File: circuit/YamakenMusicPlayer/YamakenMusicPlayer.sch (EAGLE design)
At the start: 24 parts, among them J1 DCJ0202, J2 AJ-1780, U1 NJM2396F33, U2 AE-ESP-WROOM-02

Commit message: 表記の修正
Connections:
- net DAC_GND: now also U$1.DAC_GND; no longer U$1.GND_1
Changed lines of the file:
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@@
 <part name="C4" library="rcl" library_urn="urn:adsk.eagle:library:334" deviceset="C-EU" device="050-024X044" package3d_urn="urn:adsk.eagle:package:23643/1" value="10μF"/>
 <part name="C5" library="rcl" library_urn="urn:adsk.eagle:library:334" deviceset="C-EU" device="050-024X044" package3d_urn="urn:adsk.eagle:package:23643/1" value="0.1μF"/>
-<part name="SUPPLY12" library="supply2" library_urn="urn:adsk.eagle:library:372" deviceset="GND" device=""/>
 <part name="J2" library="SamacSys_Parts" deviceset="AJ-1780" device=""/>
 <part name="SUPPLY14" library="supply2" library_urn="urn:adsk.eagle:library:372" deviceset="V+" device=""/>
@@
 <part name="JP2" library="pinhead" library_urn="urn:adsk.eagle:library:325" deviceset="PINHD-1X3" device="" package3d_urn="urn:adsk.eagle:package:22458/2" value="VOLUME_VR"/>
 <part name="U$1" library="DFPlayer_v1" deviceset="DFPLAYERMINI" device=""/>
+<part name="SUPPLY12" library="supply2" library_urn="urn:adsk.eagle:library:372" deviceset="GND" device=""/>
 </parts>
 <sheets>
@@
 <attribute name="VALUE" x="171.577" y="150.368" size="1.778" layer="96"/>
 </instance>
-<instance part="SUPPLY12" gate="GND" x="124.46" y="7.62" smashed="yes" rot="MR0">
-<attribute name="VALUE" x="47.625" y="47.625" size="1.778" layer="96" rot="MR0"/>
-</instance>
 <instance part="J2" gate="G$1" x="43.18" y="30.48" smashed="yes" rot="MR0">
 <attribute name="NAME" x="26.67" y="38.1" size="1.778" layer="95" rot="MR0" align="center-left"/>
@@
 <attribute name="NAME" x="86.36" y="38.862" size="1.4224" layer="95"/>
 <attribute name="VALUE" x="86.36" y="12.7" size="1.4224" layer="96"/>
+</instance>
+<instance part="SUPPLY12" gate="GND" x="124.46" y="7.62" smashed="yes">
+<attribute name="VALUE" x="122.555" y="4.445" size="1.778" layer="96"/>
 </instance>
 </instances>
@@
 </segment>
 <segment>
-<wire x1="116.84" y1="20.32" x2="124.46" y2="20.32" width="0.1524" layer="91"/>
-<wire x1="124.46" y1="20.32" x2="124.46" y2="10.16" width="0.1524" layer="91"/>
-<pinref part="SUPPLY12" gate="GND" pin="GND"/>
-<pinref part="U$1" gate="G$1" pin="GND_2"/>
-</segment>
-<segment>
 <pinref part="C6" gate="G$1" pin="1"/>
 <wire x1="53.34" y1="50.8" x2="48.26" y2="50.8" width="0.1524" layer="91"/>
@@
 <wire x1="175.26" y1="55.88" x2="182.88" y2="55.88" width="0.1524" layer="91"/>
 </segment>
+<segment>
+<wire x1="116.84" y1="20.32" x2="124.46" y2="20.32" width="0.1524" layer="91"/>
+<wire x1="124.46" y1="20.32" x2="124.46" y2="10.16" width="0.1524" layer="91"/>
+<pinref part="U$1" gate="G$1" pin="GND_2"/>
+<pinref part="SUPPLY12" gate="GND" pin="GND"/>
+</segment>
 </net>
 <net name="N$1" class="0">
@@
 <wire x1="48.26" y1="30.48" x2="48.26" y2="20.32" width="0.1524" layer="91"/>
 <wire x1="81.28" y1="20.32" x2="48.26" y2="20.32" width="0.1524" layer="91"/>
-<pinref part="U$1" gate="G$1" pin="GND_1"/>
-</segment>
-</net>
+<pinref part="U$1" gate="G$1" pin="DAC_GND"/>
+</segment>
+</net>

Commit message: 表記の修正
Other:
- note added: "A) 電源回路部"
- note added: "B) 制御IC部"
- note added: "C) プレイヤーIC部"
- note removed: "A 電源回路部"
- note removed: "B 制御IC部"
- note removed: "C プレイヤーIC部"
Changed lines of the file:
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@@
 <text x="241.3" y="24.13" size="1.778" layer="94">Designed by
 16TE014 中禮 大貴</text>
-<text x="106.68" y="170.18" size="2.54" layer="94">B 制御IC部</text>
-<text x="12.7" y="170.18" size="2.54" layer="94">A 電源回路部</text>
-<text x="15.24" y="66.04" size="2.54" layer="94">C プレイヤーIC部</text>
+<text x="106.68" y="170.18" size="2.54" layer="94">B) 制御IC部</text>
+<text x="12.7" y="170.18" size="2.54" layer="94">A) 電源回路部</text>
+<text x="15.24" y="66.04" size="2.54" layer="94">C) プレイヤーIC部</text>
 </plain>
 <instances>

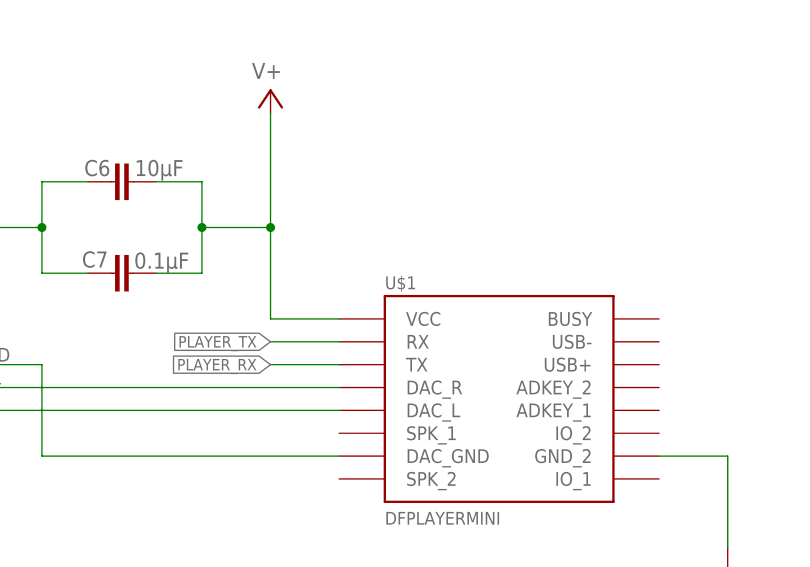
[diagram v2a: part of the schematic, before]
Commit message: U3の表記を追加
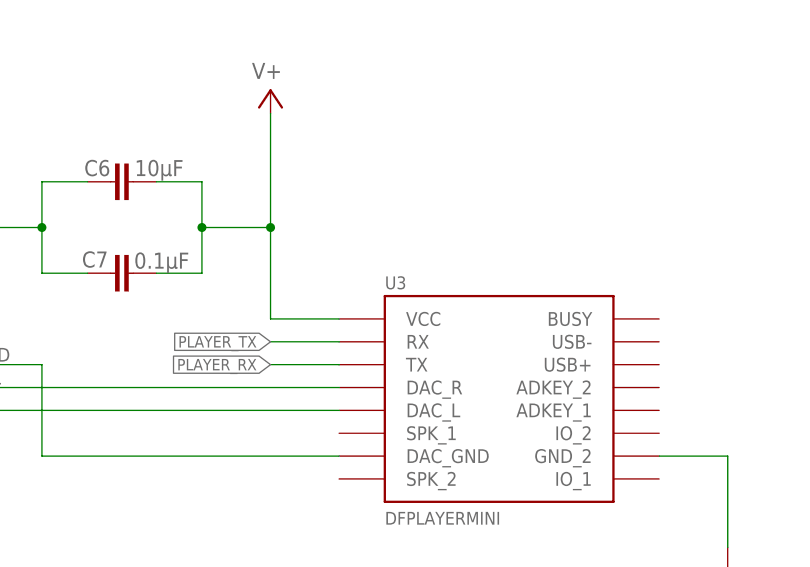
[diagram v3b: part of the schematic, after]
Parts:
- renumbered U$1 to U3
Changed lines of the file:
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@@
 <part name="SUPPLY20" library="supply2" library_urn="urn:adsk.eagle:library:372" deviceset="GND" device=""/>
 <part name="JP2" library="pinhead" library_urn="urn:adsk.eagle:library:325" deviceset="PINHD-1X3" device="" package3d_urn="urn:adsk.eagle:package:22458/2" value="VOLUME_VR"/>
-<part name="U$1" library="DFPlayer_v1" deviceset="DFPLAYERMINI" device=""/>
+<part name="U3" library="DFPlayer_v1" deviceset="DFPLAYERMINI" device=""/>
 <part name="SUPPLY12" library="supply2" library_urn="urn:adsk.eagle:library:372" deviceset="GND" device=""/>
 </parts>
@@
 <attribute name="VALUE" x="179.07" y="50.8" size="1.778" layer="96"/>
 </instance>
-<instance part="U$1" gate="G$1" x="99.06" y="25.4" smashed="yes">
+<instance part="U3" gate="G$1" x="99.06" y="25.4" smashed="yes">
 <attribute name="NAME" x="86.36" y="38.862" size="1.4224" layer="95"/>
 <attribute name="VALUE" x="86.36" y="12.7" size="1.4224" layer="96"/>
@@
 <junction x="66.04" y="45.72"/>
 <junction x="73.66" y="45.72"/>
-<pinref part="U$1" gate="G$1" pin="VCC"/>
+<pinref part="U3" gate="G$1" pin="VCC"/>
 </segment>
 <segment>
@@
 <wire x1="116.84" y1="20.32" x2="124.46" y2="20.32" width="0.1524" layer="91"/>
 <wire x1="124.46" y1="20.32" x2="124.46" y2="10.16" width="0.1524" layer="91"/>
-<pinref part="U$1" gate="G$1" pin="GND_2"/>
+<pinref part="U3" gate="G$1" pin="GND_2"/>
 <pinref part="SUPPLY12" gate="GND" pin="GND"/>
 </segment>
@@
 <wire x1="81.28" y1="33.02" x2="73.66" y2="33.02" width="0.1524" layer="91"/>
 <label x="73.66" y="33.02" size="1.27" layer="95" rot="MR0" xref="yes"/>
-<pinref part="U$1" gate="G$1" pin="RX"/>
+<pinref part="U3" gate="G$1" pin="RX"/>
 </segment>
 </net>
@@
 <wire x1="81.28" y1="30.48" x2="73.66" y2="30.48" width="0.1524" layer="91"/>
 <label x="73.66" y="30.48" size="1.27" layer="95" rot="MR0" xref="yes"/>
-<pinref part="U$1" gate="G$1" pin="TX"/>
+<pinref part="U3" gate="G$1" pin="TX"/>
 </segment>
 </net>
@@
 <pinref part="J2" gate="G$1" pin="R_1"/>
 <wire x1="81.28" y1="27.94" x2="43.18" y2="27.94" width="0.1524" layer="91"/>
-<pinref part="U$1" gate="G$1" pin="DAC_R"/>
+<pinref part="U3" gate="G$1" pin="DAC_R"/>
 </segment>
 </net>
@@
 <pinref part="J2" gate="G$1" pin="L_1"/>
 <wire x1="81.28" y1="25.4" x2="43.18" y2="25.4" width="0.1524" layer="91"/>
-<pinref part="U$1" gate="G$1" pin="DAC_L"/>
+<pinref part="U3" gate="G$1" pin="DAC_L"/>
 </segment>
 </net>
@@
 <wire x1="48.26" y1="30.48" x2="48.26" y2="20.32" width="0.1524" layer="91"/>
 <wire x1="81.28" y1="20.32" x2="48.26" y2="20.32" width="0.1524" layer="91"/>
-<pinref part="U$1" gate="G$1" pin="DAC_GND"/>
-</segment>
-</net>
+<pinref part="U3" gate="G$1" pin="DAC_GND"/>
+</segment>
+</net>

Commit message: ファイルの差し替え
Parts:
- J1: value DCJ0202 -> MJ-179PH
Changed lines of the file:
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@@
 <part name="C2" library="rcl" library_urn="urn:adsk.eagle:library:334" deviceset="CPOL-EU" device="E2.5-7" package3d_urn="urn:adsk.eagle:package:23345/1" value="22μF"/>
 <part name="3V3" library="supply2" library_urn="urn:adsk.eagle:library:372" deviceset="V+" device=""/>
-<part name="J1" library="con-jack" library_urn="urn:adsk.eagle:library:154" deviceset="DCJ0202" device="" package3d_urn="urn:adsk.eagle:package:7491/1"/>
+<part name="J1" library="con-jack" library_urn="urn:adsk.eagle:library:154" deviceset="DCJ0202" device="" package3d_urn="urn:adsk.eagle:package:7491/1" value="MJ-179PH"/>
 <part name="SUPPLY2" library="supply2" library_urn="urn:adsk.eagle:library:372" deviceset="GND" device=""/>
 <part name="R1" library="rcl" library_urn="urn:adsk.eagle:library:334" deviceset="R-EU_" device="0207/10" package3d_urn="urn:adsk.eagle:package:23491/2" value="10KΩ"/>

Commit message: 基板の修正
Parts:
- J2: value AJ-1780 -> PG203J; device SamacSys_Parts:AJ-1780 -> con-hirschmann:PG203J
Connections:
- removed net DAC_L: J2.L_1, U3.DAC_L
- new net N$2: J2.5, U3.DAC_L
- net DAC_GND: now also J2.1; no longer J2.GND
- net DAC_R: now also J2.2; no longer J2.R_1
- net N$1: now also U2.IO16
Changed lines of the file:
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@@
 <part name="C4" library="rcl" library_urn="urn:adsk.eagle:library:334" deviceset="C-EU" device="050-024X044" package3d_urn="urn:adsk.eagle:package:23643/1" value="10μF"/>
 <part name="C5" library="rcl" library_urn="urn:adsk.eagle:library:334" deviceset="C-EU" device="050-024X044" package3d_urn="urn:adsk.eagle:package:23643/1" value="0.1μF"/>
-<part name="J2" library="SamacSys_Parts" deviceset="AJ-1780" device=""/>
 <part name="SUPPLY14" library="supply2" library_urn="urn:adsk.eagle:library:372" deviceset="V+" device=""/>
 <part name="U2" library="ae-esp-wroom" deviceset="AE-ESP-WROOM-02" device=""/>
@@
 <part name="U3" library="DFPlayer_v1" deviceset="DFPLAYERMINI" device=""/>
 <part name="SUPPLY12" library="supply2" library_urn="urn:adsk.eagle:library:372" deviceset="GND" device=""/>
+<part name="J2" library="con-hirschmann" library_urn="urn:adsk.eagle:library:153" deviceset="PG203J" device="" package3d_urn="urn:adsk.eagle:package:7447/1"/>
 </parts>
 <sheets>
@@
 <attribute name="VALUE" x="171.577" y="150.368" size="1.778" layer="96"/>
 </instance>
-<instance part="J2" gate="G$1" x="43.18" y="30.48" smashed="yes" rot="MR0">
-<attribute name="NAME" x="26.67" y="38.1" size="1.778" layer="95" rot="MR0" align="center-left"/>
-<attribute name="VALUE" x="26.67" y="35.56" size="1.778" layer="96" rot="MR0" align="center-left"/>
-</instance>
 <instance part="SUPPLY14" gate="1" x="73.66" y="60.96" smashed="yes" rot="MR0">
 <attribute name="VALUE" x="74.93" y="62.23" size="1.778" layer="96" rot="MR0"/>
@@
 <instance part="SUPPLY12" gate="GND" x="124.46" y="7.62" smashed="yes">
 <attribute name="VALUE" x="122.555" y="4.445" size="1.778" layer="96"/>
+</instance>
+<instance part="J2" gate="1" x="25.4" y="30.48" smashed="yes" rot="MR0">
+<attribute name="NAME" x="33.02" y="34.29" size="1.778" layer="95" rot="MR0"/>
+<attribute name="VALUE" x="33.02" y="20.32" size="1.778" layer="96" rot="MR0"/>
 </instance>
 </instances>
@@
 <segment>
 <pinref part="R1" gate="G$1" pin="1"/>
-<wire x1="215.9" y1="147.32" x2="215.9" y2="132.08" width="0.1524" layer="91"/>
+<wire x1="215.9" y1="147.32" x2="215.9" y2="137.16" width="0.1524" layer="91"/>
+<wire x1="215.9" y1="137.16" x2="215.9" y2="132.08" width="0.1524" layer="91"/>
 <wire x1="215.9" y1="132.08" x2="195.58" y2="132.08" width="0.1524" layer="91"/>
 <pinref part="S2" gate="1" pin="S"/>
@@
 <junction x="215.9" y="132.08"/>
 <pinref part="U2" gate="G$1" pin="RST"/>
+<pinref part="U2" gate="G$1" pin="IO16"/>
+<wire x1="195.58" y1="137.16" x2="215.9" y2="137.16" width="0.1524" layer="91"/>
+<junction x="215.9" y="137.16"/>
 </segment>
 </net>
@@
 <net name="DAC_R" class="0">
 <segment>
-<pinref part="J2" gate="G$1" pin="R_1"/>
 <wire x1="81.28" y1="27.94" x2="43.18" y2="27.94" width="0.1524" layer="91"/>
 <pinref part="U3" gate="G$1" pin="DAC_R"/>
-</segment>
-</net>
-<net name="DAC_L" class="0">
-<segment>
-<pinref part="J2" gate="G$1" pin="L_1"/>
-<wire x1="81.28" y1="25.4" x2="43.18" y2="25.4" width="0.1524" layer="91"/>
-<pinref part="U3" gate="G$1" pin="DAC_L"/>
+<wire x1="43.18" y1="27.94" x2="43.18" y2="25.4" width="0.1524" layer="91"/>
+<pinref part="J2" gate="1" pin="2"/>
+<wire x1="43.18" y1="25.4" x2="38.1" y2="25.4" width="0.1524" layer="91"/>
 </segment>
 </net>
 <net name="DAC_GND" class="0">
 <segment>
-<pinref part="J2" gate="G$1" pin="GND"/>
-<wire x1="43.18" y1="30.48" x2="48.26" y2="30.48" width="0.1524" layer="91"/>
-<wire x1="48.26" y1="30.48" x2="48.26" y2="20.32" width="0.1524" layer="91"/>
-<wire x1="81.28" y1="20.32" x2="48.26" y2="20.32" width="0.1524" layer="91"/>
+<wire x1="38.1" y1="22.86" x2="43.18" y2="22.86" width="0.1524" layer="91"/>
+<wire x1="43.18" y1="22.86" x2="43.18" y2="20.32" width="0.1524" layer="91"/>
+<wire x1="81.28" y1="20.32" x2="43.18" y2="20.32" width="0.1524" layer="91"/>
 <pinref part="U3" gate="G$1" pin="DAC_GND"/>
+<pinref part="J2" gate="1" pin="1"/>
 </segment>
 </net>
@@
 <segment>
 <pinref part="U2" gate="G$1" pin="TOUT"/>
-<wire x1="195.58" y1="134.62" x2="205.74" y2="134.62" width="0.1524" layer="91"/>
-<label x="205.74" y="134.62" size="1.27" layer="95" xref="yes"/>
+<wire x1="195.58" y1="134.62" x2="220.98" y2="134.62" width="0.1524" layer="91"/>
+<label x="220.98" y="134.62" size="1.27" layer="95" xref="yes"/>
 </segment>
 <segment>
@@
 </segment>
 </net>
+<net name="N$2" class="0">
+<segment>
+<pinref part="J2" gate="1" pin="5"/>
+<wire x1="38.1" y1="33.02" x2="45.72" y2="33.02" width="0.1524" layer="91"/>
+<wire x1="45.72" y1="33.02" x2="45.72" y2="25.4" width="0.1524" layer="91"/>
+<pinref part="U3" gate="G$1" pin="DAC_L"/>
+<wire x1="45.72" y1="25.4" x2="81.28" y2="25.4" width="0.1524" layer="91"/>
+</segment>
+</net>
